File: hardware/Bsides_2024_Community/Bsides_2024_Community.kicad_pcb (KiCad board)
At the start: 2 copper layers, 169.6 x 159.5 mm, 45 parts, among them J1 Add_On, J2 Battery, J3 Battery, J4 OLED, J5 Serial_IN, J6 Serial_OUT, P1 USB_C_Plug_USB2.0, Q1 DMG3415U-7, SW1 ON, SW2 RESET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

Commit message: feat(Hw): Labels added
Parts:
- added kibuzzard-666B3243: G***, kibuzzard-666B3243, B.Cu at (142.6, 131.8)
- added kibuzzard-666B3258: G***, kibuzzard-666B3258, B.Cu at (142.6, 155.0)
- added kibuzzard-666B327A: G***, kibuzzard-666B327A, B.Cu at (133.4, 143.5)
- added kibuzzard-666B55CA: G***, kibuzzard-666B55CA, B.Cu at (150.8, 143.5)
- added kibuzzard-666B5A62: G***, kibuzzard-666B5A62, F.Cu at (206.3, 150.2)
- added kibuzzard-666B5A62: G***, kibuzzard-666B5A62, B.Cu at (72.2, 167.6)
- added kibuzzard-666B5A91: G***, kibuzzard-666B5A91, F.Cu at (208.1, 148.6)
- added kibuzzard-666B5A91: G***, kibuzzard-666B5A91, B.Cu at (73.8, 169.7)
- added kibuzzard-666B5AA1: G***, kibuzzard-666B5AA1, F.Cu at (210.1, 146.5)
- added kibuzzard-666B5AA1: G***, kibuzzard-666B5AA1, B.Cu at (70.9, 165.3)
- added kibuzzard-666B5BCA: G***, kibuzzard-666B5BCA, B.Cu at (107.5, 78.7)
- added kibuzzard-666B5C0A: G***, kibuzzard-666B5C0A, B.Cu at (112.1, 85.2)
- added kibuzzard-666B5C24: G***, kibuzzard-666B5C24, B.Cu at (109.1, 76.8)
- added kibuzzard-666B5C33: G***, kibuzzard-666B5C33, B.Cu at (114.5, 84.1)
- J6: moved to B.Cu
- moved SW2 0.07 mm to (91.3, 134.1)
- turned J6 to 37.296 degrees
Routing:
- net GND: track 38.3 -> 46.9 mm, vias 28 -> 34

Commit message: feat(Hw):Update_PCB_Community
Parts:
- added kibuzzard-666C6473: G***, kibuzzard-666C6473, B.Cu at (203.2, 129.6)
- added kibuzzard-666C64A5: G***, kibuzzard-666C64A5, B.Cu at (197.8, 122.5)
- added kibuzzard-666C65B2: G***, kibuzzard-666C65B2, B.Cu at (91.3, 150.1)
- added kibuzzard-666C65C9: G***, kibuzzard-666C65C9, B.Cu at (91.1, 138.5)
- added kibuzzard-666C6629: G***, kibuzzard-666C6629, B.Cu at (111.1, 74.9)
- added kibuzzard-666C6636: G***, kibuzzard-666C6636, B.Cu at (116.7, 83.2)
- added kibuzzard-666C6653: G***, kibuzzard-666C6653, B.Cu at (133.3, 98.8)
- added kibuzzard-666C6676: G***, kibuzzard-666C6676, B.Cu at (150.4, 98.8)
- moved C3 5.88 mm to (96.4, 148.0)
- moved SW3 4.33 mm to (91.4, 146.5)
- moved C11 1.45 mm to (147.7, 129.4)
- moved kibuzzard-666B5C33 0.65 mm to (114.0, 84.4)
- moved kibuzzard-666B5C0A 0.59 mm to (111.5, 85.2)
- moved SW1 0.26 mm to (203.6, 124.1)
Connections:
- net /GPIO16 renamed /TX
- net /GPIO17 renamed /RX
- net /GPIO4 renamed /RX1
- net /GPIO5 renamed /TX1
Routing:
- net /BOOT: track 47.0 -> 51.5 mm
- net Net-(D3-DOUT): track 146.3 -> 148.0 mm
- net Net-(D2-DOUT): track 50.1 -> 51.7 mm
- net GND: track 46.9 -> 47.8 mm
- net /VOUT: track 411.0 -> 411.7 mm
- net +BATT: track 81.2 -> 81.9 mm

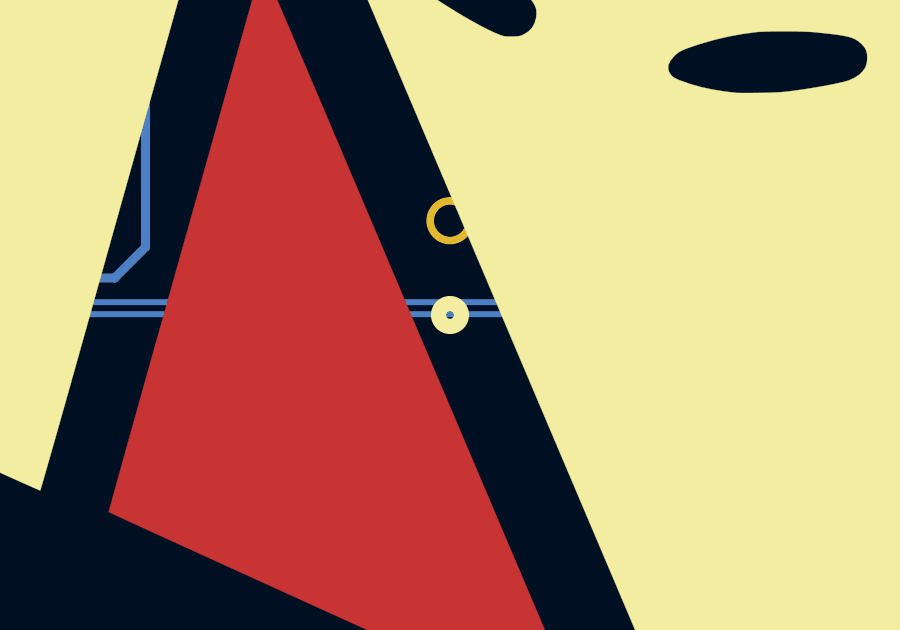
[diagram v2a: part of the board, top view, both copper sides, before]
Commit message: feat(Hw):Update_Guest_SCH_Labels
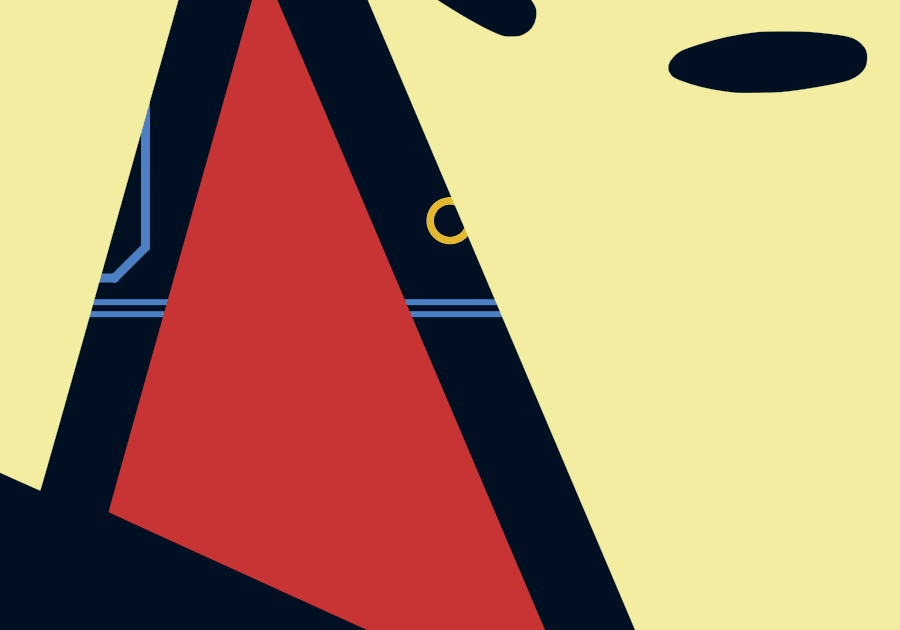
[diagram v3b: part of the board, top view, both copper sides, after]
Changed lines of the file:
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@@
 			(layer "B.SilkS")
-		)
-		(fp_circle
-			(center 3.142895 0)
-			(end 3.523895 0)
-			(stroke
-				(width 0.508)
-				(type solid)
-			)
-			(fill none)
-			(layer "B.SilkS")
-		)
-		(fp_circle
-			(center 3.142895 0)
-			(end 3.523895 0)
-			(stroke
-				(width 0.508)
-				(type solid)
-			)
-			(fill none)
-			(layer "F.SilkS")
 		)
 		(fp_line

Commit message: feat(hw): add logos community
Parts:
- added G***: LOGO, LOGO, B.Cu at (162.1, 130.4)
- added G***: LOGO, LOGO, B.Cu at (142.4, 109.5)
- added REF**: OSHW-Logo_7.5x8mm_SilkScreen, Symbol:OSHW-Logo_7.5x8mm_SilkScreen, B.Cu at (172.5, 84.7)
- added kibuzzard-666C8E87: G***, kibuzzard-666C8E87, B.Cu at (143.0, 104.0)
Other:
- board text added: "4e6576657220676f6e6e612067 69766520796f752075700a4e65 76657220676f6e6e61206c6574 20796f7520646f776e0a4e6576 657220676f6e6e612072756e20 61726f756e6420616e64206465 7365727420796f75"
- board text added: "Aqui inicia el tour por latinoamerica Parce Wey Che"
- board text added: "Elige tu bando, rudo o tecnico?"
- board text added: "Lucharan de 2 a 3 caidas sin limite de tiempo!!"

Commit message: feat(hw): add labels
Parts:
- removed kibuzzard-666B5C24: G***, kibuzzard-666B5C24
- removed kibuzzard-666B5C33: G***, kibuzzard-666B5C33
- added kibuzzard-666C95B8: G***, kibuzzard-666C95B8, B.Cu at (114.0, 84.4)
- added kibuzzard-666C95BF: G***, kibuzzard-666C95BF, B.Cu at (109.1, 76.8)
